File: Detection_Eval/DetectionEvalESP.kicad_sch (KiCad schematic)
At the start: 4 parts, among them J2 USB_A, U6 ESP8266

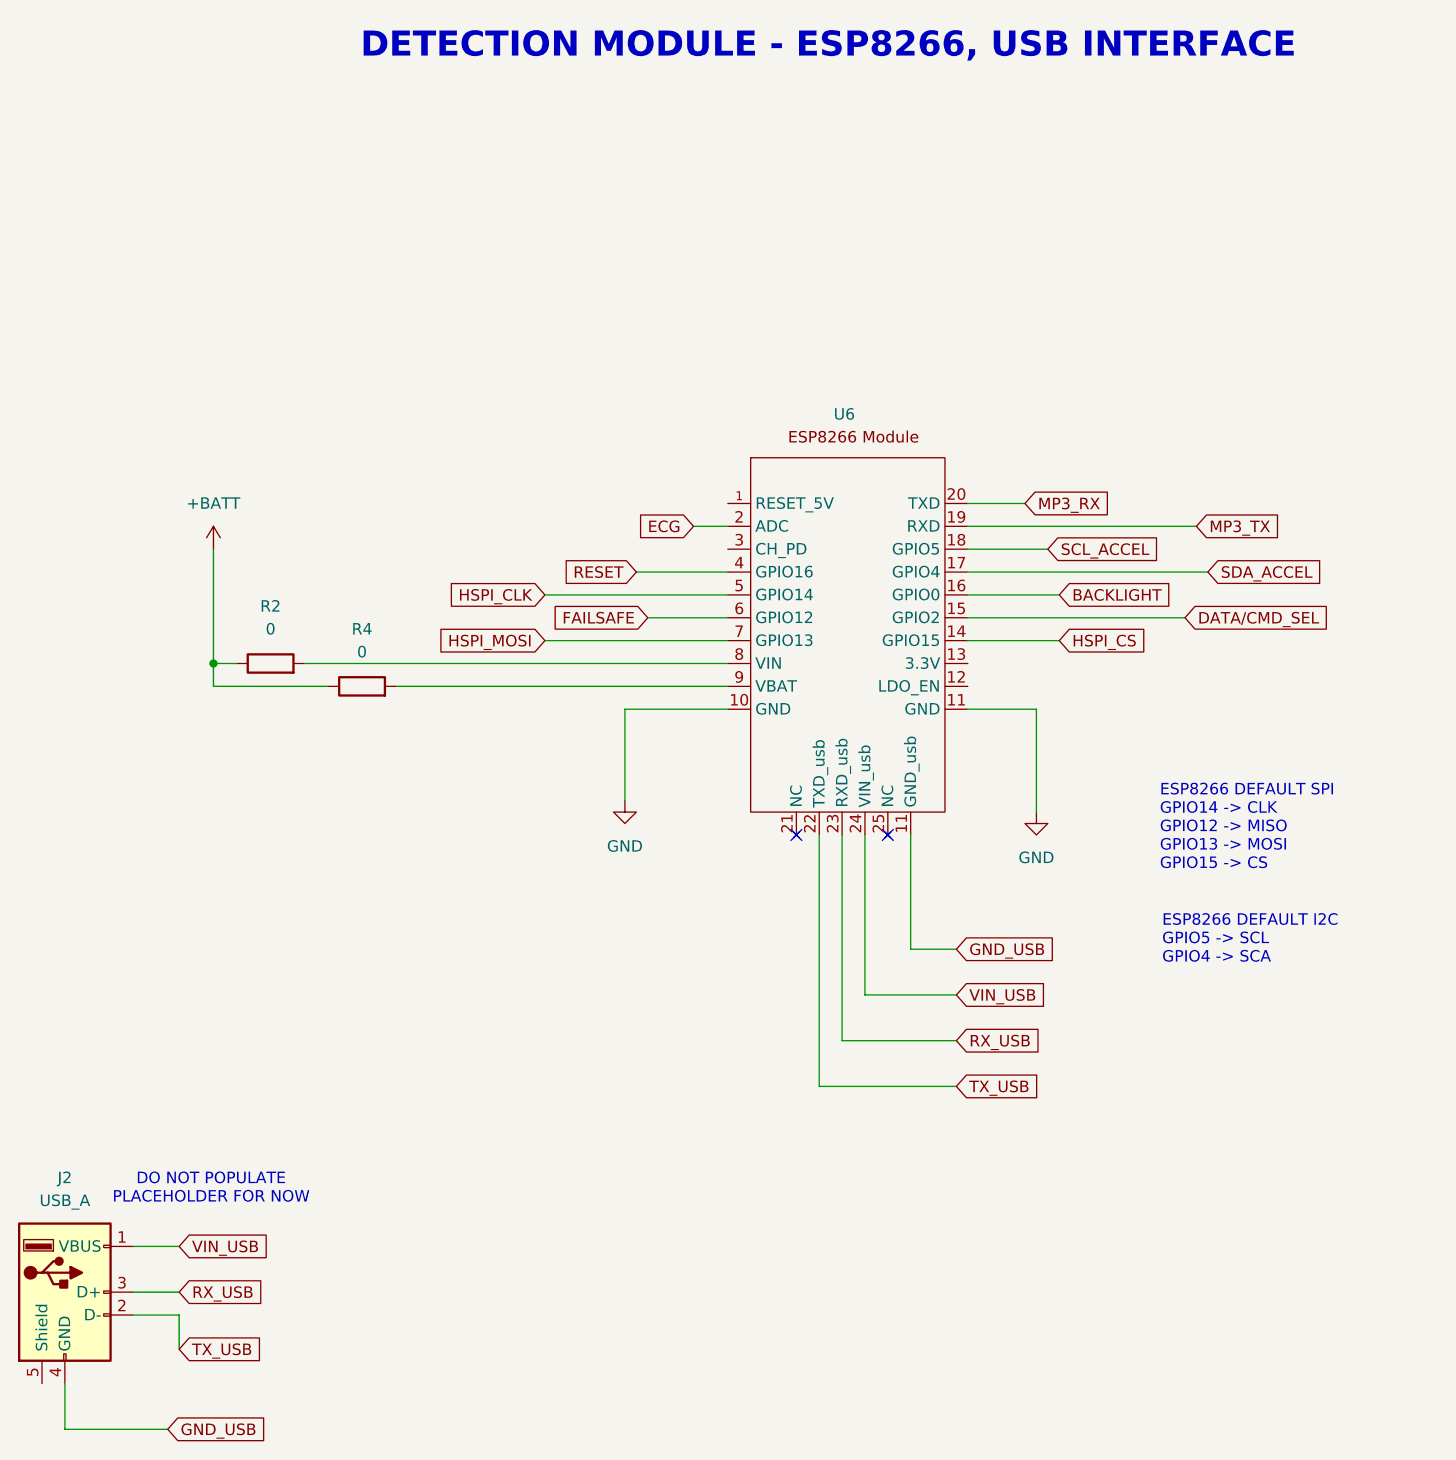
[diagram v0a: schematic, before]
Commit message: Madison_02-04
Battery added
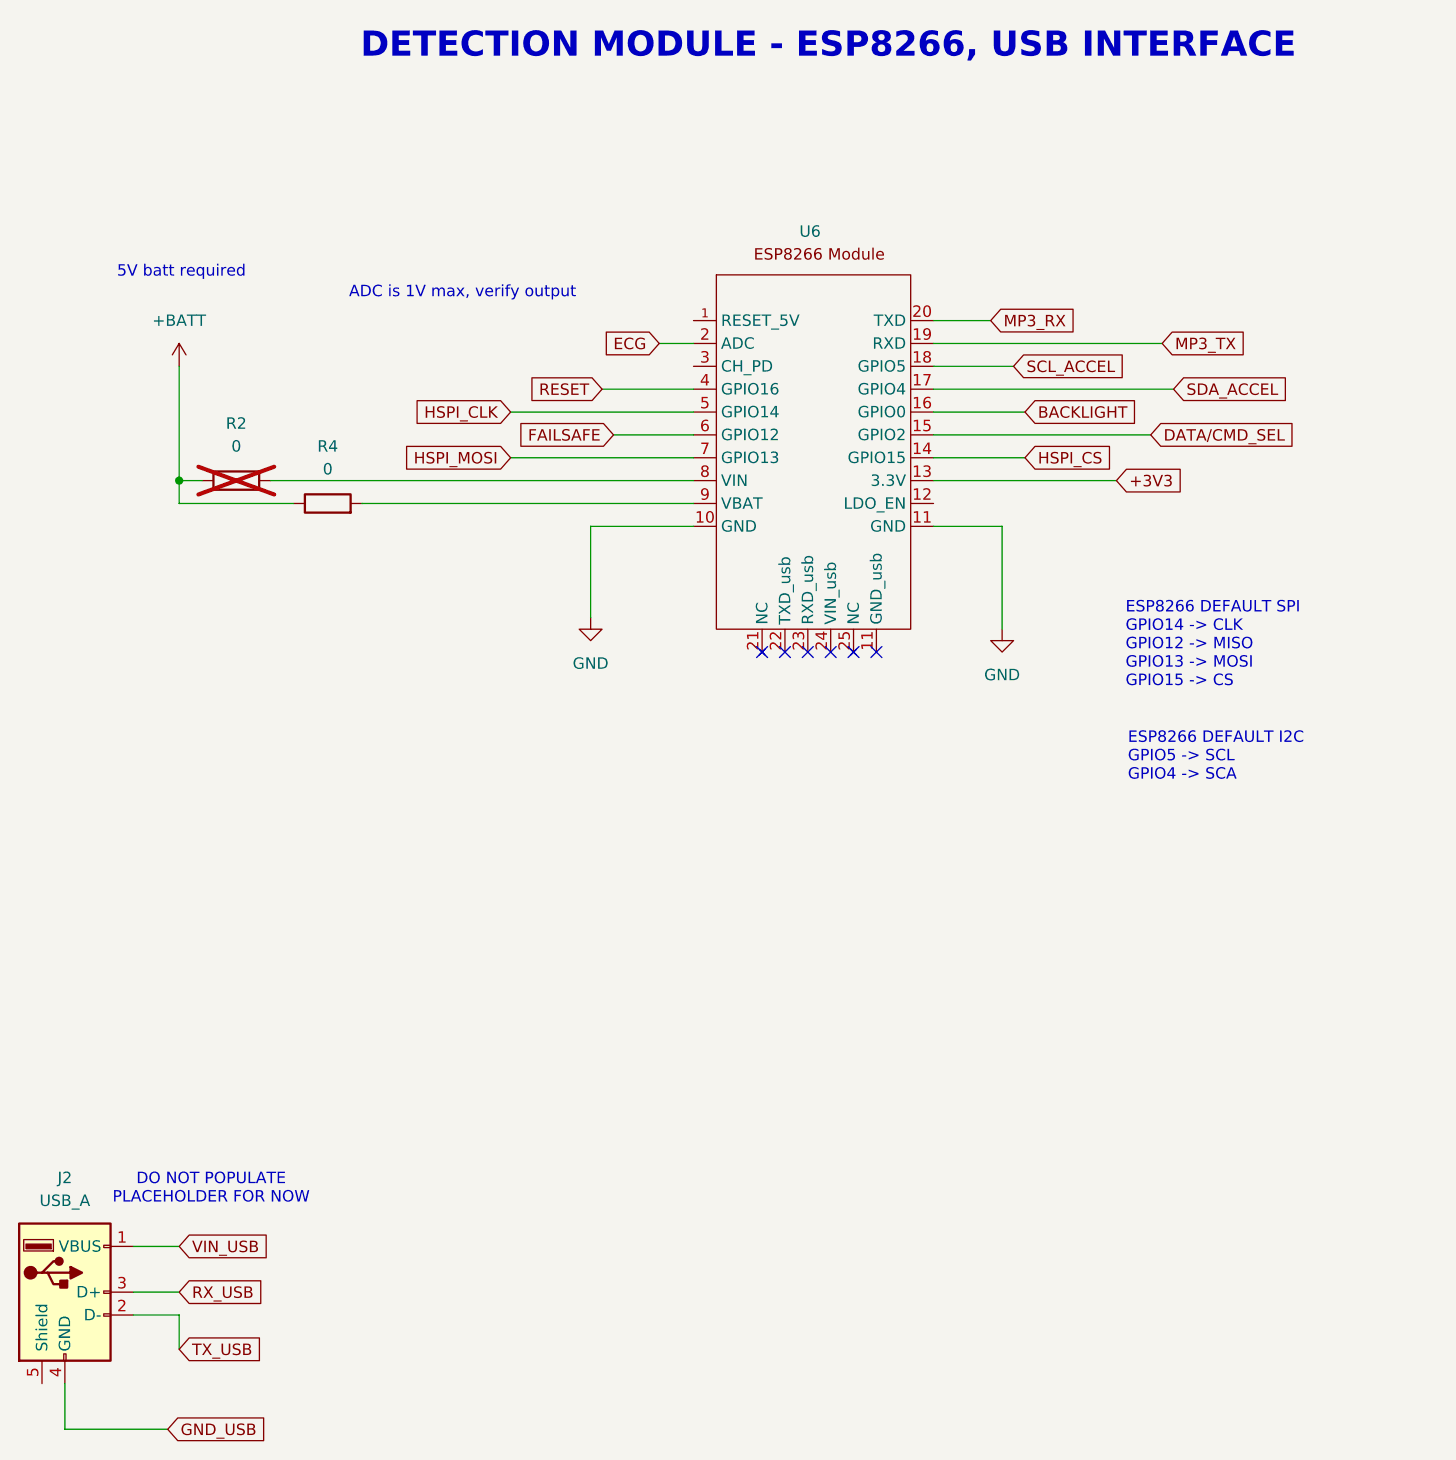
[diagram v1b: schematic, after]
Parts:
- R2: now not fitted
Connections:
- net GND_USB: no longer U6.11 (GND_usb)
- net RX_USB: no longer U6.23 (RXD_usb)
- net TX_USB: no longer U6.22 (TXD_usb)
- net VIN_USB: no longer U6.24 (VIN_usb)
- net +3V3: now reaches U6.13 (3.3V)
- no-connect marks 2 -> 6
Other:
- note added: "5V batt required"
- note added: "ADC is 1V max, verify output"
- moved on the sheet: R4, U6

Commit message: Madison_02-05
1.2V to 5V battery regulator added
chose AAAA 600maH rechargeable battery
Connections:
- net +BATT renamed +5V
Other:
- note added: "ADC Pin, 1V max ECG Signal 0V - 0.992V"
- note removed: "5V batt required"
- note removed: "ADC is 1V max, verify output"

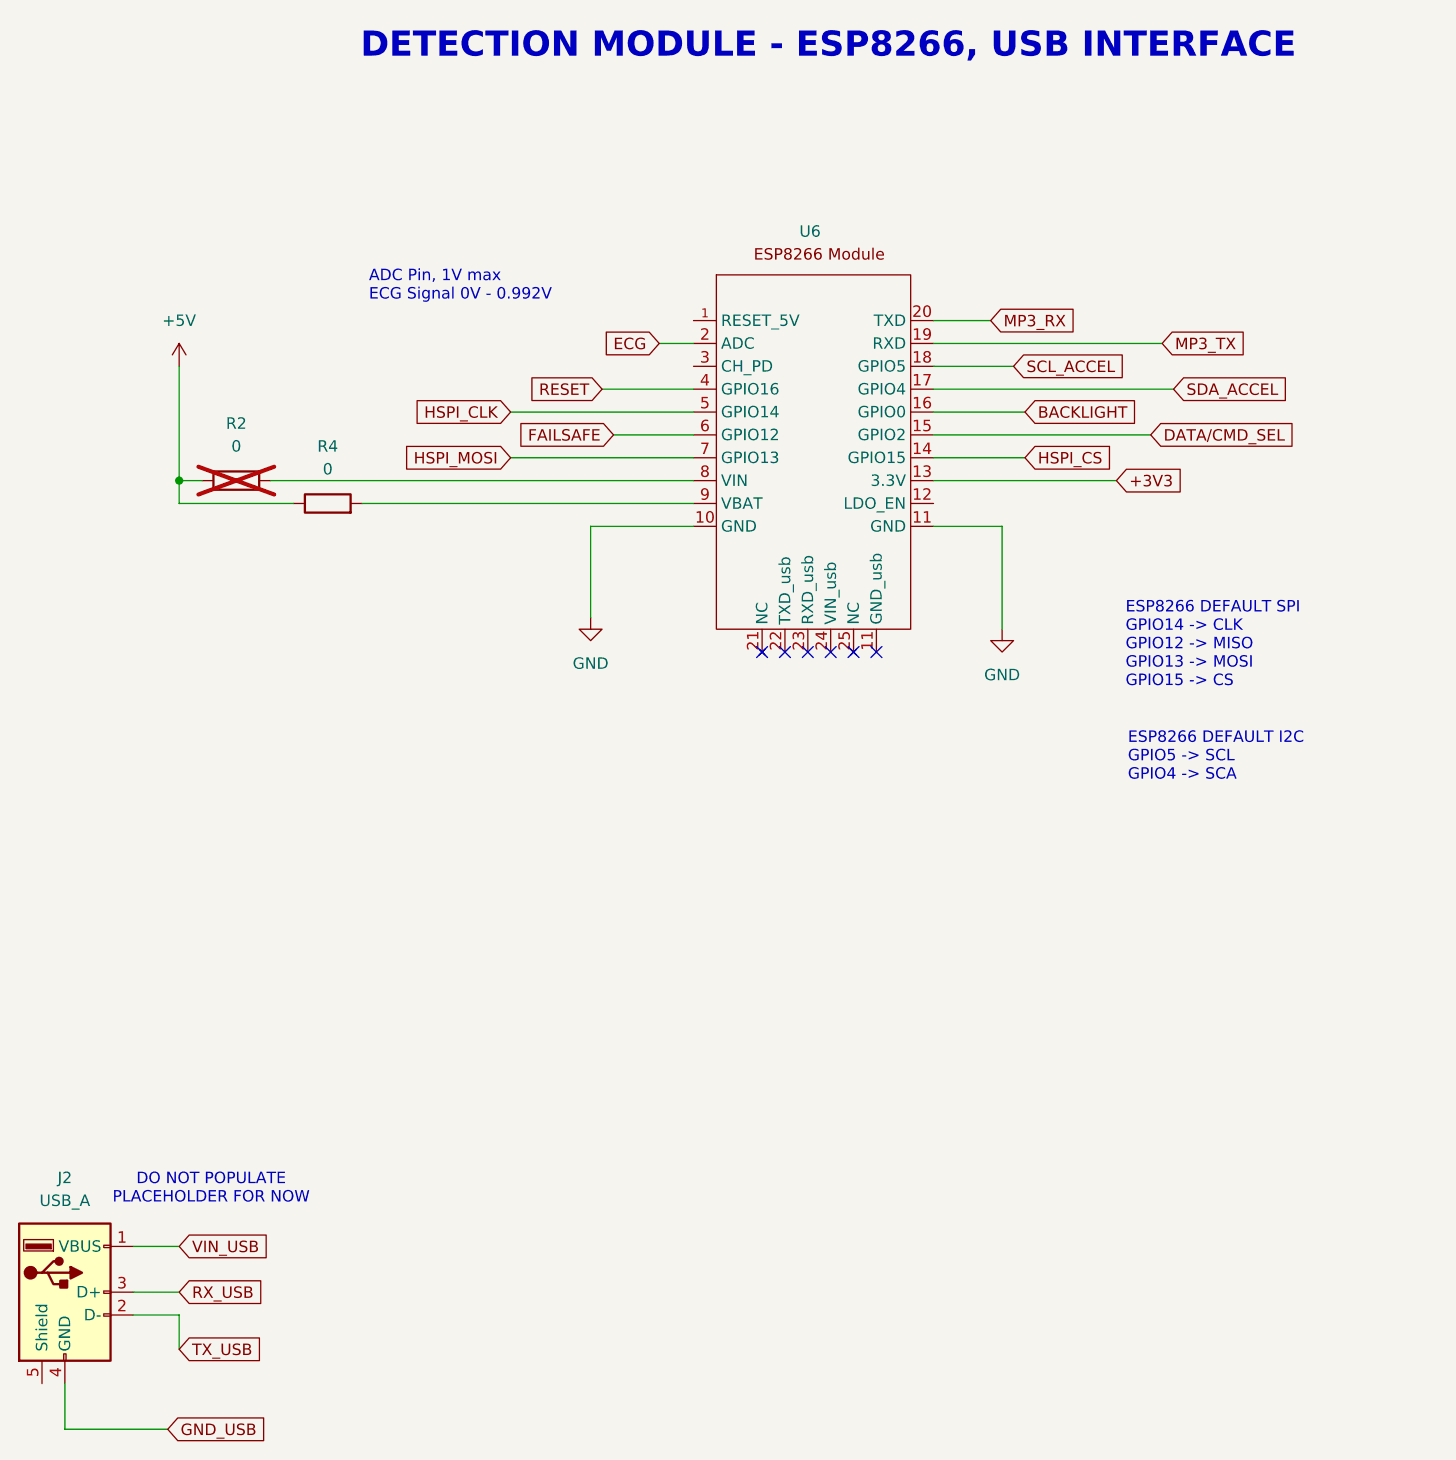
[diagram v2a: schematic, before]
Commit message: Madison_02-05_2
Added battery charger circuit
Added footprints to accelerometer, lcd screen, buttons, AND gate, batt charger, batt holder
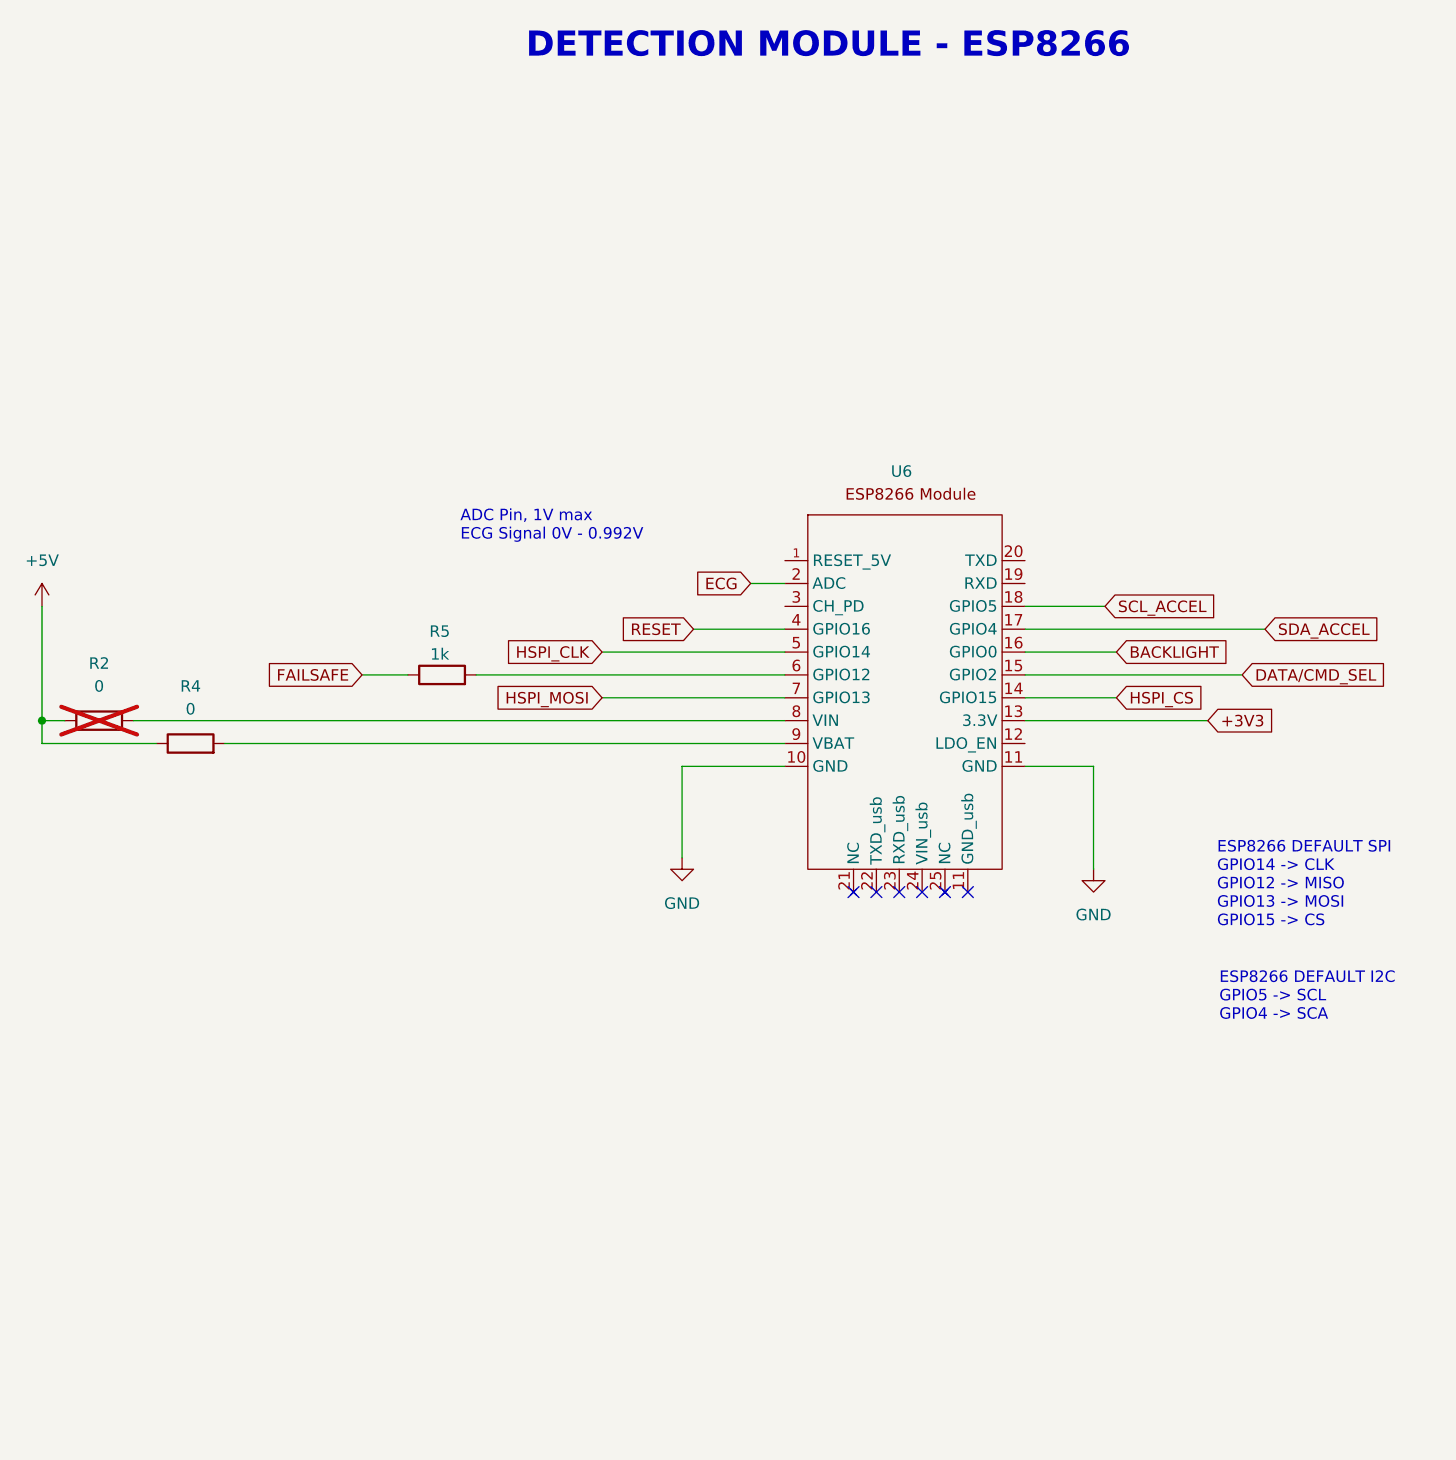
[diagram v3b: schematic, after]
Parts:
- removed J2: USB_A, symbol Connector:USB_A
- added R5: 1k, Resistor_SMD:R_0402_1005Metric, symbol Device:R
- U6: footprint (none) -> Module:Adafruit_HUZZAH_ESP8266_breakout_WithMountingHoles
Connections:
- net FAILSAFE: now also R5.1; no longer U6.6 (GPIO12)
- net MP3_RX: no longer names the net of U6.20 (TXD)
- net MP3_TX: no longer names the net of U6.19 (RXD)
- new net: R5.2, U6.6 (GPIO12)
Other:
- note added: "DETECTION MODULE - ESP8266"
- note removed: "DETECTION MODULE - ESP8266, USB INTERFACE"
- note removed: "DO NOT POPULATE PLACEHOLDER FOR NOW"
- moved on the sheet: R2, R4, U6

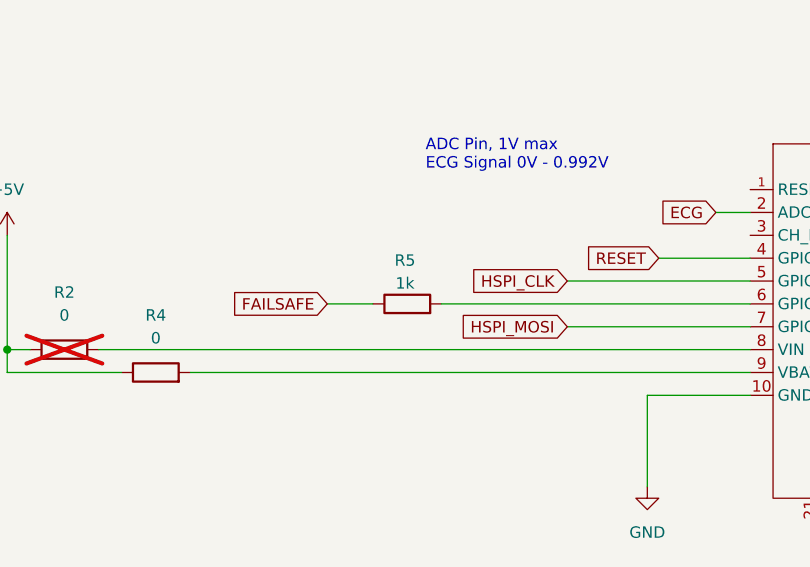
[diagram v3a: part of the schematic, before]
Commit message: Madison_02-06
final footprints added and layout positioning mostly done
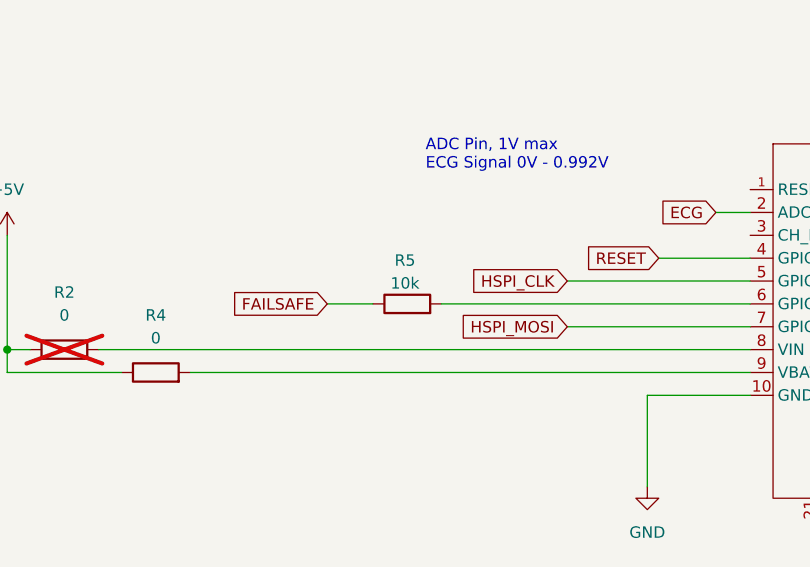
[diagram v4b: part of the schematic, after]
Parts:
- R5: value 1k -> 10k
- U6: footprint Module:Adafruit_HUZZAH_ESP8266_breakout_WithMountingHoles -> Module:Adafruit_HUZZAH_ESP8266_breakout
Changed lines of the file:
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@@
 			)
 		)
-		(property "Footprint" "Module:Adafruit_HUZZAH_ESP8266_breakout_WithMountingHoles"
+		(property "Footprint" "Module:Adafruit_HUZZAH_ESP8266_breakout"
 			(at 146.05 99.06 0)
 			(effects
@@
 			)
 		)
-		(property "Value" "1k"
+		(property "Value" "10k"
 			(at 97.536 87.884 90)
 			(effects
